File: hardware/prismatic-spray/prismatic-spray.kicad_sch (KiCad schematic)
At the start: 17 parts, among them J1 Conn_01x03_Male, J2 Conn_01x03_Male, SW1 SW_Push, SW2 SW_Push, SW3 SW_Push, SW4 SW_Push, SW5 RotaryEncoder_Switch, U1 Pico

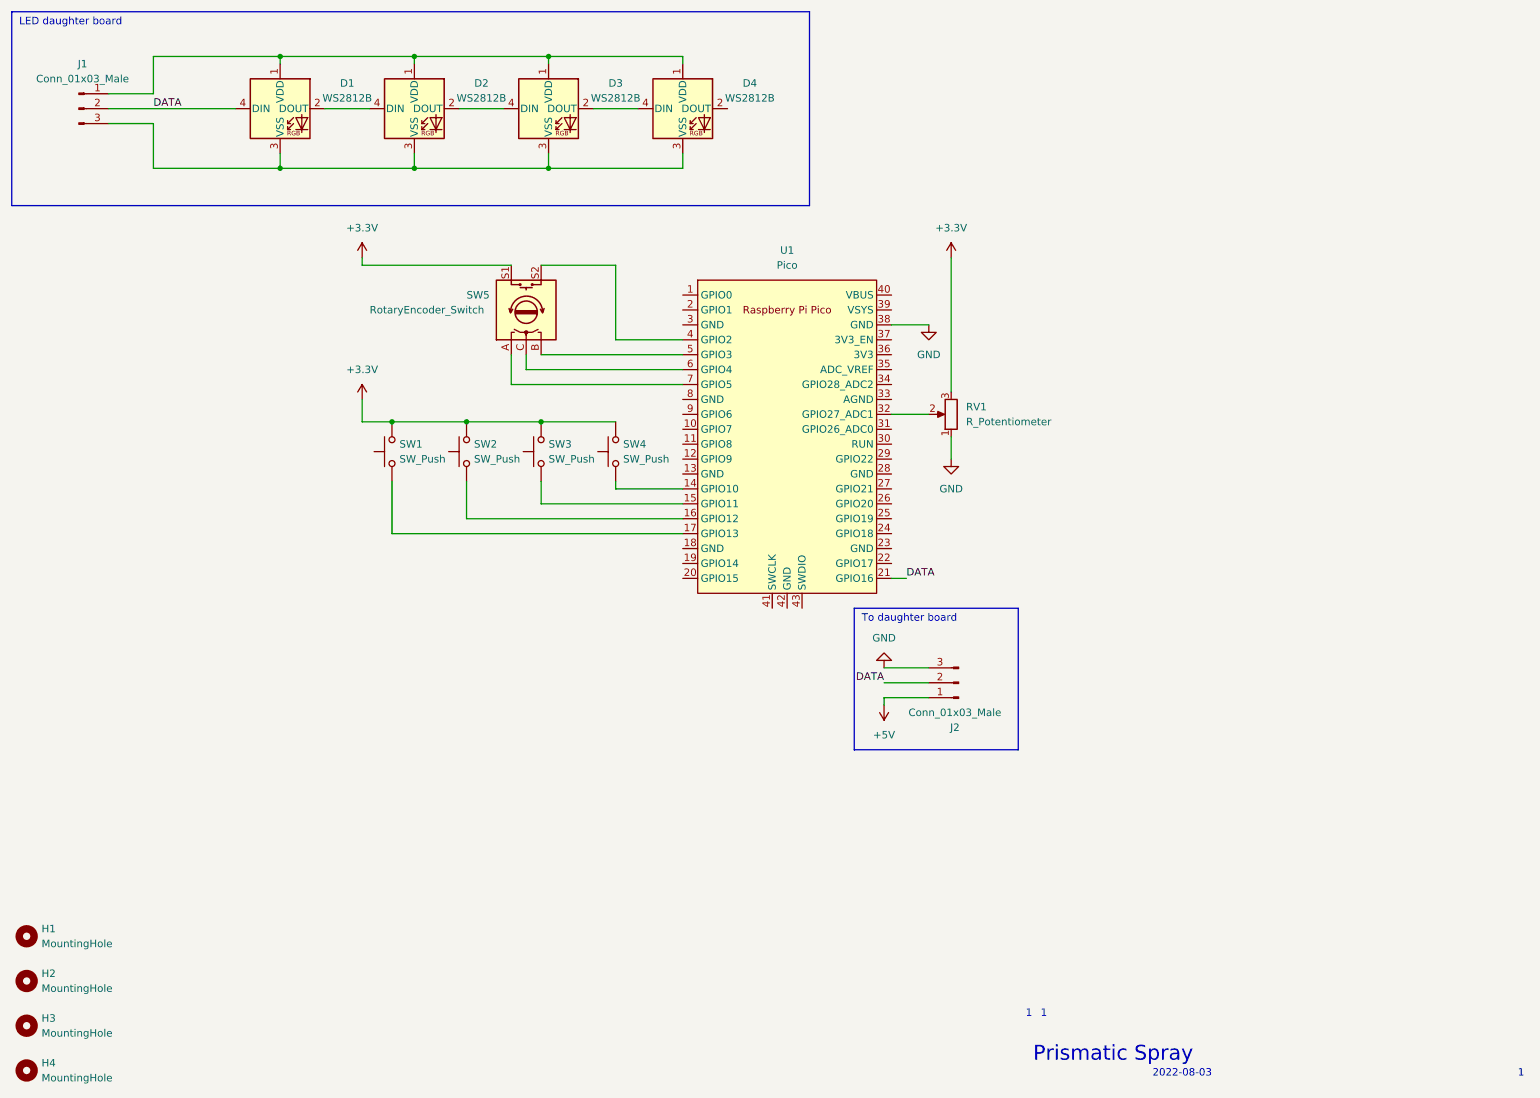
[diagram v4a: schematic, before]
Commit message: Route most traces
- Route most traces on main board and daughter board
- Add mounting holes to daughter board
- Flip daughterboard connector to back of PCB
- Reassign some GPIOs for better routing
- Fix footprint for pec11 to get clean DRC
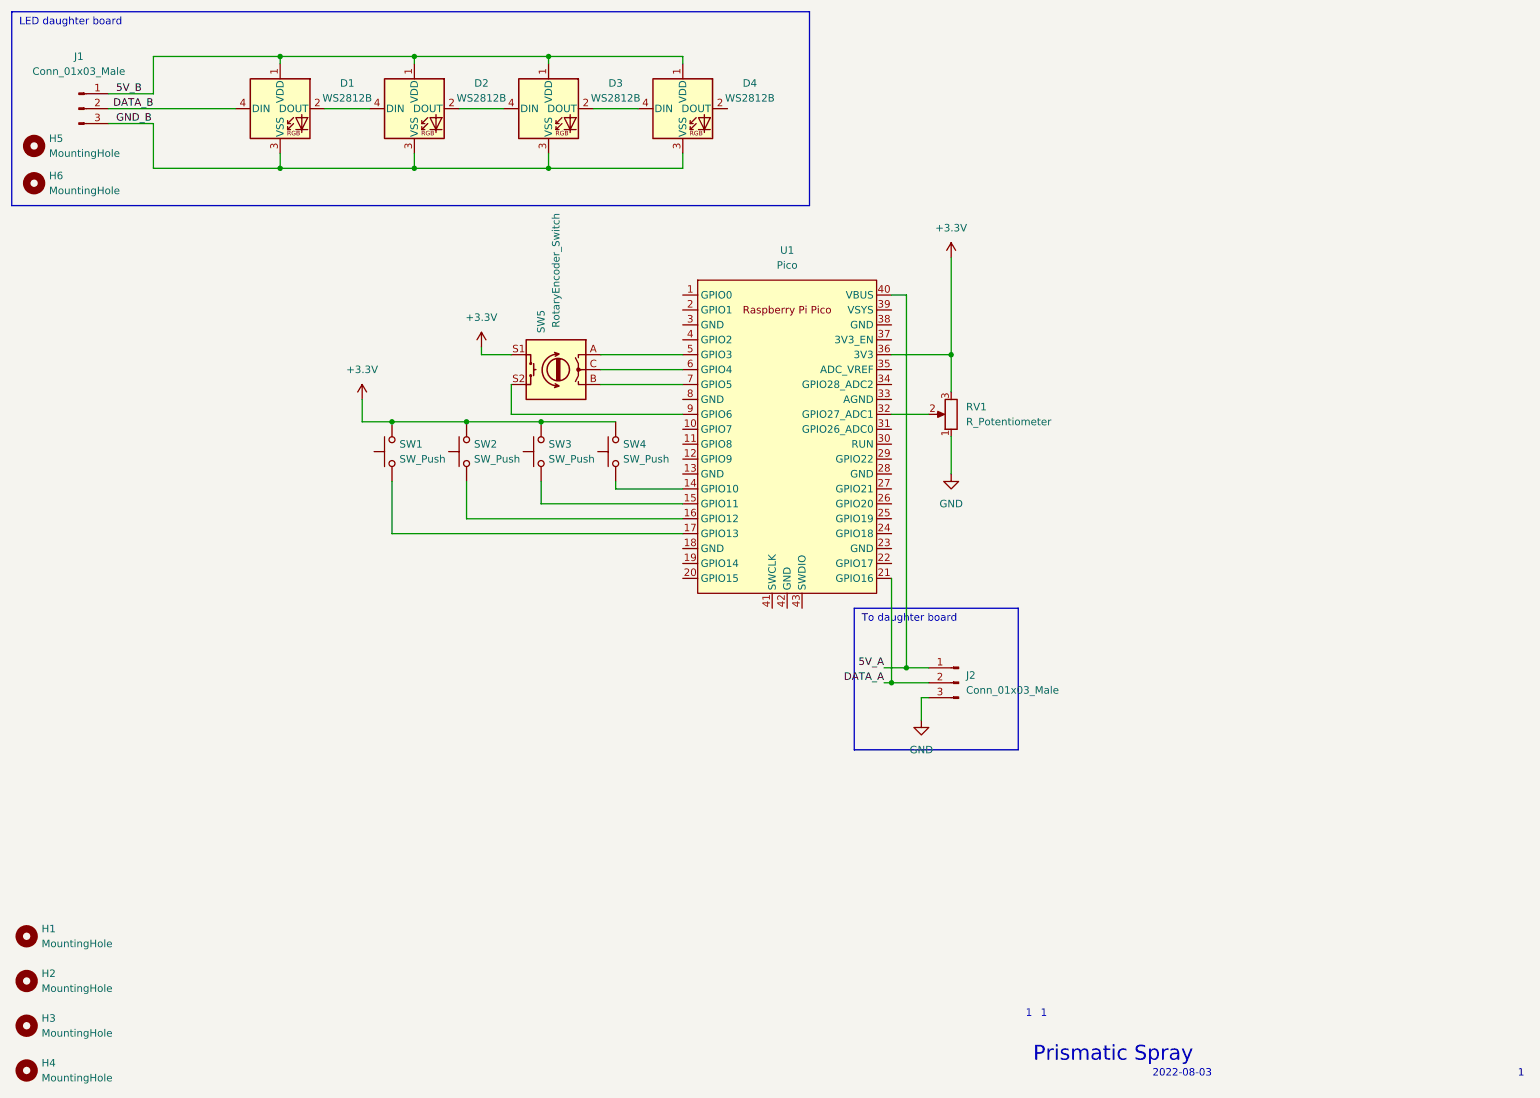
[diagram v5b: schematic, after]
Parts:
- added H5, H6: MountingHole, MountingHole:MountingHole_2.7mm_M2.5, symbol Mechanical:MountingHole
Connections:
- net +5V is gone; now on net 5V_A: J2.1 (Pin_1)
- net +3V3: now also U1.36 (3V3)
- net GND: no longer U1.38 (GND)
- net at SW5.A: now also U1.5 (GPIO3); no longer U1.7 (GPIO5)
- net at SW5.B: now also U1.7 (GPIO5); no longer U1.5 (GPIO3)
- net at SW5.S2: now also U1.9 (GPIO6); no longer U1.4 (GPIO2)
- net 5V_A: now reaches U1.40 (VBUS)
- net 5V_B: now reaches D1.1 (VDD), D2.1 (VDD), D3.1 (VDD), D4.1 (VDD), J1.1 (Pin_1)
- net GND_B: now reaches D1.3 (VSS), D2.3 (VSS), D3.3 (VSS), D4.3 (VSS), J1.3 (Pin_3)
- net DATA renamed DATA_A
- net DATA_A: no longer D1.4 (DIN), J1.2 (Pin_2)
- new net DATA_B: D1.4 (DIN), J1.2 (Pin_2)
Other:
- moved on the sheet: J2, SW5

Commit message: Separate boards into different schematics
KiCAD: 1 board = 1 project

So sayeth the forums:
https://forum.kicad.info/t/hooking-up-a-separate-board-to-the-main-one-with-a-cable/37093
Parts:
- removed D1, D2, D3, D4: WS2812B, LED_SMD:LED_WS2812B_PLCC4_5.0x5.0mm_P3.2mm, symbol LED:WS2812B
- removed H5, H6: MountingHole, MountingHole:MountingHole_2.7mm_M2.5, symbol Mechanical:MountingHole
- removed J1, J2: Conn_01x03_Male, Connector_JST:JST_PH_S3B-PH-K_1x03_P2.00mm_Horizontal, symbol Connector:Conn_01x03_Male
- added J?: Conn_01x04_Male, symbol Connector:Conn_01x04_Male
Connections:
- net GND: now also J?.2 (Pin_2), J?.4 (Pin_4)
- net 5V_A renamed 5V
- net 5V: now also J?.1 (Pin_1)
- net DATA_A renamed DATA
- net DATA: now also J?.3 (Pin_3)
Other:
- note removed: "LED daughter board"
